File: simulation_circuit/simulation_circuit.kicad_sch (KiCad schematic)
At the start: 0 parts

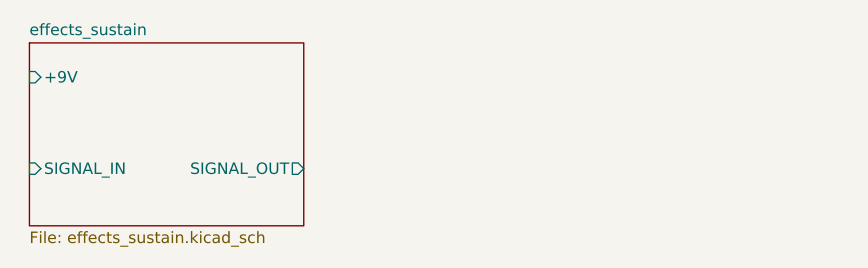
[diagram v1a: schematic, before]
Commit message: added LTSpice standard diode library to SPICE sim library, copied and simulated envelope effect, WIP determining if isolated or chained sim behaviour is correct
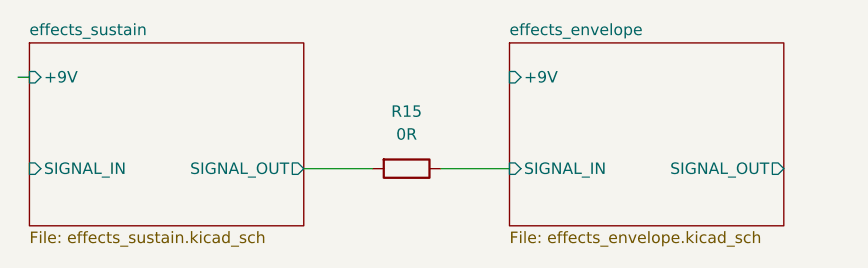
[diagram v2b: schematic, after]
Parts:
- added R15: 0R, symbol Device:R
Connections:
- net effects_sustain/SIGNAL_OUT: now also R15.2
- new net effects_envelope/SIGNAL_IN: R15.1
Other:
- added sheet effects_envelope (effects_envelope.kicad_sch)
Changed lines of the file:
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@@
 (kicad_sch (version 20211123) (generator eeschema)
   (paper "A4")
+  (wire (pts (xy 129.54 80.01) (xy 128.27 80.01))
+    (stroke (width 0) (type default) (color 0 0 0 0))
+  )
+  (wire (pts (xy 160.02 90.17) (xy 167.64 90.17))
+    (stroke (width 0) (type default) (color 0 0 0 0))
+  )
+  (wire (pts (xy 175.26 90.17) (xy 182.88 90.17))
+    (stroke (width 0) (type default) (color 0 0 0 0))
+  )
+  (symbol (lib_id "Device:R") (at 171.45 90.17 270) (unit 1)
+    (in_bom yes) (on_board yes) (fields_autoplaced)
+    (property "Reference" "R15" (id 0) (at 171.45 83.82 90))
+    (property "Value" "0R" (id 1) (at 171.45 86.36 90))
+    (property "Footprint" "" (id 2) (at 171.45 88.392 90)
+      (effects (font (size 1.27 1.27)) hide)
+    )
+    (property "Datasheet" "~" (id 3) (at 171.45 90.17 0)
+      (effects (font (size 1.27 1.27)) hide)
+    )
+    (pin "1")
+    (pin "2")
+  )
   (sheet (at 129.54 76.2) (size 30.48 20.32) (fields_autoplaced)
     (stroke (width 0.1524) (type solid) (color 0 0 0 0))
@@
     )
   )
+  (sheet (at 182.88 76.2) (size 30.48 20.32) (fields_autoplaced)
+    (stroke (width 0.1524) (type solid) (color 0 0 0 0))
+    (fill (color 0 0 0 0.0000))
+    (property "Sheet name" "effects_envelope" (id 0) (at 182.88 75.4884 0)
+      (effects (font (size 1.27 1.27)) (justify left bottom))
+    )
+    (property "Sheet file" "effects_envelope.kicad_sch" (id 1) (at 182.88 97.1046 0)
+      (effects (font (size 1.27 1.27)) (justify left top))
+    )
+    (pin "+9V" input (at 182.88 80.01 180)
+      (effects (font (size 1.27 1.27)) (justify left))
+    )
+    (pin "SIGNAL_OUT" output (at 213.36 90.17 0)
+      (effects (font (size 1.27 1.27)) (justify right))
+    )
+    (pin "SIGNAL_IN" input (at 182.88 90.17 180)
+      (effects (font (size 1.27 1.27)) (justify left))
+    )
+  )
   (sheet_instances
     (path "/" (page "1"))
     (path "/526e42b9-dcb2-4f91-83ee-1d25bf9d2787" (page "2"))
+    (path "/e6e2e2d2-b923-48d0-be33-59979c2e35eb" (page "3"))
   )
   (symbol_instances
@@
       (reference "#GND03") (unit 1) (value "0") (footprint "")
     )
+    (path "/e6e2e2d2-b923-48d0-be33-59979c2e35eb/4a1d52b1-4976-4d17-964f-dda50b6fad80"
+      (reference "#GND?") (unit 1) (value "0") (footprint "")
+    )
+    (path "/e6e2e2d2-b923-48d0-be33-59979c2e35eb/7878a6fe-6858-466f-9f56-c1f8dd2ec94d"
+      (reference "#GND?") (unit 1) (value "0") (footprint "")
+    )
     (path "/526e42b9-dcb2-4f91-83ee-1d25bf9d2787/b59a32d9-c8ed-4da6-aba6-5f7bf09d4309"
       (reference "#PWR01") (unit 1) (value "GND") (footprint "")
+    )
+    (path "/e6e2e2d2-b923-48d0-be33-59979c2e35eb/31ed097b-5a20-4e2f-937b-e1393697bade"
+      (reference "#PWR?") (unit 1) (value "GND") (footprint "")
     )
     (path "/526e42b9-dcb2-4f91-83ee-1d25bf9d2787/a5e9747d-329e-4d3e-8455-ae1d70409960"
@@
       (reference "C4") (unit 1) (value "0.1uF") (footprint "")
     )
+    (path "/e6e2e2d2-b923-48d0-be33-59979c2e35eb/e051c90c-7f94-450c-8423-6e59c778f485"
+      (reference "C5") (unit 1) (value "1uF") (footprint "")
+    )
+    (path "/e6e2e2d2-b923-48d0-be33-59979c2e35eb/2726859c-a968-43dc-b7d9-5bd63a5da55c"
+      (reference "C6") (unit 1) (value "500pF") (footprint "")
+    )
+    (path "/e6e2e2d2-b923-48d0-be33-59979c2e35eb/d7fcc530-b16c-41dd-800c-2dca768a55a2"
+      (reference "C7") (unit 1) (value "0.1uF") (footprint "")
+    )
+    (path "/e6e2e2d2-b923-48d0-be33-59979c2e35eb/ace55088-c4b2-4762-b18f-6c5debc62d13"
+      (reference "D1") (unit 1) (value "1N914") (footprint "Diode_THT:D_DO-35_SOD27_P7.62mm_Horizontal")
+    )
+    (path "/e6e2e2d2-b923-48d0-be33-59979c2e35eb/e3c1b771-a445-477b-ac34-1a544079affd"
+      (reference "D2") (unit 1) (value "1N914") (footprint "Diode_THT:D_DO-35_SOD27_P7.62mm_Horizontal")
+    )
     (path "/526e42b9-dcb2-4f91-83ee-1d25bf9d2787/c199f0b4-8741-4ede-b3b0-1a50f6638fb9"
       (reference "Q1") (unit 1) (value "BC547") (footprint "Package_TO_SOT_THT:TO-92_Inline")
+    )
+    (path "/e6e2e2d2-b923-48d0-be33-59979c2e35eb/ee8ceb34-94ad-41f6-b9d7-5d0f2c5da6e3"
+      (reference "Q2") (unit 1) (value "BC547B") (footprint "Package_TO_SOT_THT:TO-92_Inline")
     )
     (path "/526e42b9-dcb2-4f91-83ee-1d25bf9d2787/fd99880c-32e1-4366-b100-ba42f7a7bb8b"
@@
       (reference "R9") (unit 1) (value "8.2kR") (footprint "")
     )
+    (path "/e6e2e2d2-b923-48d0-be33-59979c2e35eb/63d80d20-c655-48e1-a7b2-7a4793f4a960"
+      (reference "R10") (unit 1) (value "100kR") (footprint "")
+    )
+    (path "/e6e2e2d2-b923-48d0-be33-59979c2e35eb/b6d19e34-a28b-4016-a6c7-3d360b9715e0"
+      (reference "R11") (unit 1) (value "470kR") (footprint "")
+    )
+    (path "/e6e2e2d2-b923-48d0-be33-59979c2e35eb/273fd1ce-2452-4503-b426-4e2e4887680e"
+      (reference "R12") (unit 1) (value "15kR") (footprint "")
+    )
+    (path "/e6e2e2d2-b923-48d0-be33-59979c2e35eb/42391954-a263-4072-9d44-11ba3b086a65"
+      (reference "R13") (unit 1) (value "100R") (footprint "")
+    )
+    (path "/e6e2e2d2-b923-48d0-be33-59979c2e35eb/5f8cebff-71c1-476a-a27a-d485c4e63bdd"
+      (reference "R14") (unit 1) (value "8.2kR") (footprint "")
+    )
+    (path "/2916d8a1-abd6-4fab-b3c3-bd04a683e5bf"
+      (reference "R15") (unit 1) (value "0R") (footprint "")
+    )
     (path "/526e42b9-dcb2-4f91-83ee-1d25bf9d2787/8ce95041-64f8-4a9f-bad7-dd0098a2290d"
       (reference "V1") (unit 1) (value "VSIN") (footprint "")
@@
       (reference "V2") (unit 1) (value "VDC") (footprint "")
     )
+    (path "/e6e2e2d2-b923-48d0-be33-59979c2e35eb/f33a2818-b151-4e23-af27-81de837d407c"
+      (reference "V3") (unit 1) (value "VSIN") (footprint "")
+    )
+    (path "/e6e2e2d2-b923-48d0-be33-59979c2e35eb/ca536ca6-57ae-4727-ac0f-652a2eb7759c"
+      (reference "V4") (unit 1) (value "VDC") (footprint "")
+    )
   )
